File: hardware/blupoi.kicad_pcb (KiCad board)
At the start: 2 copper layers, 229.7 x 29.5 mm, 133 parts, among them P1 MICRO-B-USB, SW1 PM_BTN, U1 NRF52832, U2 TPS63031DSKR, U3 bno055, U4 ics43432, U5 BQ24075RGTT, U6 MAX16054AZT+T, U7 sip32408, X1 32MHz

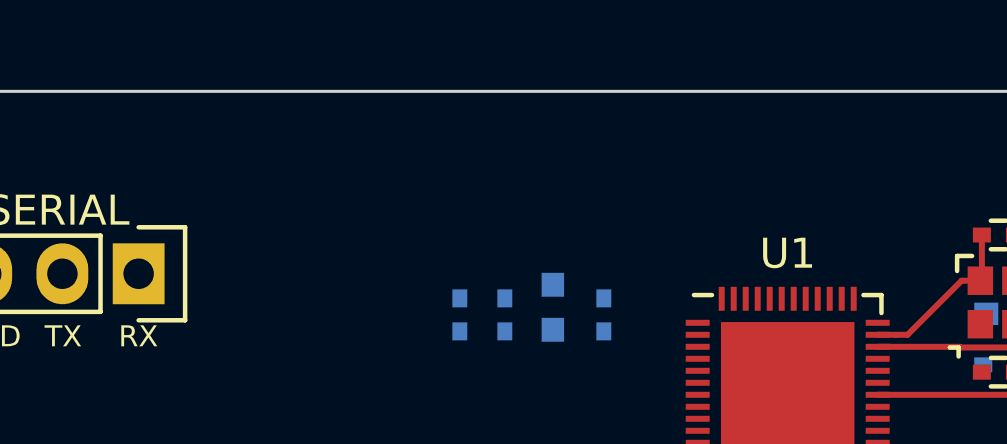
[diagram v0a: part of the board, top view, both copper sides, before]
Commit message: Added mode button
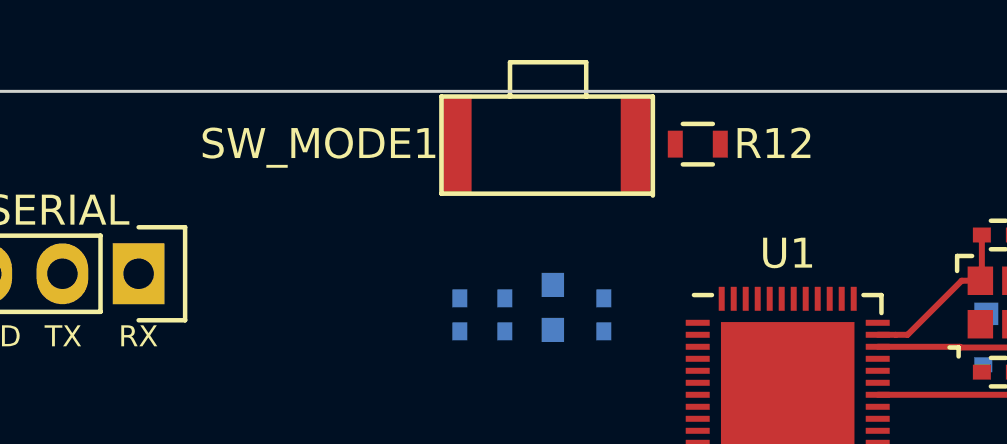
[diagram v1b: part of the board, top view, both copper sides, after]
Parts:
- added R12: 10k, Resistors_SMD:R_0603, F.Cu at (10.6, 94.9)
- added SW_MODE1: SW_SPST, kss241glfs:KSS241GLFS, F.Cu at (9.14, 96.5)
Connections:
- U6 pad 3: Net-(U6-Pad3) -> PM_SWITCH
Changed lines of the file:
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@@
-(kicad_pcb (version 20170123) (host pcbnew no-vcs-found-7652~57~ubuntu16.10.1)
+(kicad_pcb (version 20170123) (host pcbnew no-vcs-found-7663~57~ubuntu16.10.1)
   (general
-    (links 508)
-    (no_connects 436)
+    (links 512)
+    (no_connects 439)
     (area -60.860001 93.069999 168.980001 122.650001)
     (thickness 1.6)
@@
     (tracks 133)
     (zones 0)
-    (modules 133)
-    (nets 236)
+    (modules 135)
+    (nets 235)
   )
   (page A4)
@@
   )
   (setup
-    (last_trace_width 0.85)
+    (last_trace_width 0.2)
     (user_trace_width 0.2)
     (user_trace_width 0.25)
@@
   (net 226 "Net-(U3-Pad3)")
   (net 227 "Net-(U5-Pad14)")
-  (net 228 "Net-(U6-Pad3)")
-  (net 229 "Net-(U6-Pad4)")
-  (net 230 "Net-(U6-Pad5)")
-  (net 231 "Net-(U1-Pad11)")
-  (net 232 "Net-(U1-Pad12)")
-  (net 233 "Net-(U2-Pad4)")
-  (net 234 "Net-(U2-Pad2)")
-  (net 235 "Net-(U7-Pad2)")
+  (net 228 "Net-(U6-Pad4)")
+  (net 229 "Net-(U6-Pad5)")
+  (net 230 "Net-(U1-Pad11)")
+  (net 231 "Net-(U2-Pad4)")
+  (net 232 "Net-(U2-Pad2)")
+  (net 233 "Net-(U7-Pad2)")
+  (net 234 "Net-(R12-Pad1)")
   (net_class Default "This is the default net class."
     (clearance 0.2)
@@
     (add_net "Net-(R1-Pad1)")
     (add_net "Net-(R10-Pad1)")
+    (add_net "Net-(R12-Pad1)")
     (add_net "Net-(R2-Pad1)")
     (add_net "Net-(R3-Pad1)")
@@
     (add_net "Net-(U1-Pad10)")
     (add_net "Net-(U1-Pad11)")
-    (add_net "Net-(U1-Pad12)")
     (add_net "Net-(U1-Pad20)")
     (add_net "Net-(U1-Pad22)")
@@
     (add_net "Net-(U3-Pad6)")
     (add_net "Net-(U5-Pad14)")
-    (add_net "Net-(U6-Pad3)")
     (add_net "Net-(U6-Pad4)")
     (add_net "Net-(U6-Pad5)")
@@
       (net 212 "Net-(U1-Pad10)"))
     (pad 11 smd rect (at -3 1.8) (size 0.8 0.2) (layers F.Cu F.Paste F.Mask)
-      (net 231 "Net-(U1-Pad11)"))
+      (net 230 "Net-(U1-Pad11)"))
     (pad 12 smd rect (at -3 2.2) (size 0.8 0.2) (layers F.Cu F.Paste F.Mask)
-      (net 232 "Net-(U1-Pad12)") (clearance 0.001))
+      (net 234 "Net-(R12-Pad1)") (clearance 0.001))
     (pad 13 smd rect (at -2.2 3 90) (size 0.8 0.2) (layers F.Cu F.Paste F.Mask)
       (net 186 V3.3))
@@
       (net 184 VIN))
     (pad 4 smd oval (at 0.5 1.55 90) (size 0.28 1) (layers F.Cu F.Paste F.Mask)
-      (net 233 "Net-(U2-Pad4)"))
+      (net 231 "Net-(U2-Pad4)"))
     (pad 3 smd oval (at 0 1.55 90) (size 0.28 1) (layers F.Cu F.Paste F.Mask)
       (net 2 GND))
     (pad 2 smd oval (at -0.5 1.55 90) (size 0.28 1) (layers F.Cu F.Paste F.Mask)
-      (net 234 "Net-(U2-Pad2)"))
+      (net 232 "Net-(U2-Pad2)"))
     (pad 1 smd oval (at -1 1.55 90) (size 0.28 1) (layers F.Cu F.Paste F.Mask)
       (net 186 V3.3))
@@
       (net 2 GND) (clearance 0.14986))
     (pad 3 smd rect (at 0.94996 1.19888 180) (size 0.50038 0.8001) (layers F.Cu F.Paste F.Mask)
-      (net 228 "Net-(U6-Pad3)") (clearance 0.14986))
+      (net 192 PM_SWITCH) (clearance 0.14986))
     (pad 6 smd rect (at -0.94996 -1.19888 180) (size 0.50038 0.8001) (layers F.Cu F.Paste F.Mask)
       (net 185 VBAT) (clearance 0.14986))
     (pad 4 smd rect (at 0.94996 -1.19888 180) (size 0.50038 0.8001) (layers F.Cu F.Paste F.Mask)
-      (net 229 "Net-(U6-Pad4)") (clearance 0.14986))
+      (net 228 "Net-(U6-Pad4)") (clearance 0.14986))
     (pad 5 smd rect (at 0 -1.19888 180) (size 0.50038 0.8001) (layers F.Cu F.Paste F.Mask)
-      (net 230 "Net-(U6-Pad5)") (clearance 0.14986))
+      (net 229 "Net-(U6-Pad5)") (clearance 0.14986))
     (model ${KISYS3DMOD}/TO_SOT_Packages_SMD.3dshapes/SOT-23-6.wrl
       (at (xyz 0 0 0))
@@
     )
     (pad 2 smd rect (at -0.895 1.65 270) (size 0.3 0.7) (layers F.Cu F.Paste F.Mask)
-      (net 235 "Net-(U7-Pad2)"))
+      (net 233 "Net-(U7-Pad2)"))
     (pad 1 smd rect (at -0.395 1.65 270) (size 0.3 0.7) (layers F.Cu F.Paste F.Mask)
       (net 202 VCHG))
@@
       (net 184 VIN))
     (pad 3 smd rect (at -0.895 0 270) (size 0.3 0.7) (layers F.Cu F.Paste F.Mask)
-      (net 230 "Net-(U6-Pad5)"))
+      (net 229 "Net-(U6-Pad5)"))
     (pad 1 smd rect (at -0.645 0.825 270) (size 0.86 0.5) (layers F.Cu F.Paste F.Mask)
       (net 202 VCHG))
@@
     )
   )
+  (module Resistors_SMD:R_0603 (layer F.Cu)
+    (at 10.64 94.88)
+    (descr "Resistor SMD 0603, reflow soldering, Vishay (see dcrcw.pdf)")
+    (tags "resistor 0603")
+    (attr smd)
+    (fp_text reference R12 (at 2.54 0) (layer F.SilkS)
+      (effects (font (size 1 1) (thickness 0.15)))
+    )
+    (fp_text value 10k (at 0 1.9) (layer F.Fab)
+      (effects (font (size 1 1) (thickness 0.15)))
+    )
+    (fp_line (start -0.5 -0.675) (end 0.5 -0.675) (layer F.SilkS) (width 0.15))
+    (fp_line (start 0.5 0.675) (end -0.5 0.675) (layer F.SilkS) (width 0.15))
+    (fp_line (start 1.3 -0.8) (end 1.3 0.8) (layer F.CrtYd) (width 0.05))
+    (fp_line (start -1.3 -0.8) (end -1.3 0.8) (layer F.CrtYd) (width 0.05))
+    (fp_line (start -1.3 0.8) (end 1.3 0.8) (layer F.CrtYd) (width 0.05))
+    (fp_line (start -1.3 -0.8) (end 1.3 -0.8) (layer F.CrtYd) (width 0.05))
+    (fp_line (start -0.8 -0.4) (end 0.8 -0.4) (layer F.Fab) (width 0.1))
+    (fp_line (start 0.8 -0.4) (end 0.8 0.4) (layer F.Fab) (width 0.1))
+    (fp_line (start 0.8 0.4) (end -0.8 0.4) (layer F.Fab) (width 0.1))
+    (fp_line (start -0.8 0.4) (end -0.8 -0.4) (layer F.Fab) (width 0.1))
+    (pad 2 smd rect (at 0.75 0) (size 0.5 0.9) (layers F.Cu F.Paste F.Mask)
+      (net 2 GND))
+    (pad 1 smd rect (at -0.75 0) (size 0.5 0.9) (layers F.Cu F.Paste F.Mask)
+      (net 234 "Net-(R12-Pad1)"))
+    (model Resistors_SMD.3dshapes/R_0603.wrl
+      (at (xyz 0 0 0))
+      (scale (xyz 1 1 1))
+      (rotate (xyz 0 0 0))
+    )
+  )
+  (module kss241glfs:KSS241GLFS (layer F.Cu)
+    (at 9.1415 96.531 180)
+    (fp_text reference SW_MODE1 (at 11.1125 1.651 180) (layer F.SilkS)
+      (effects (font (size 1 1) (thickness 0.15)))
+    )
+    (fp_text value SW_SPST (at 0 -0.635 180) (layer F.Fab)
+      (effects (font (size 1 1) (thickness 0.15)))
+    )
+    (fp_line (start 4.7625 4.3815) (end 2.2225 4.3815) (layer F.SilkS) (width 0.15))
+    (fp_line (start 2.2225 4.3815) (end 2.2225 3.2385) (layer F.SilkS) (width 0.15))
+    (fp_line (start 4.7625 3.2385) (end 4.7625 4.3815) (layer F.SilkS) (width 0.15))
+    (fp_line (start 7.0485 0) (end 0 0) (layer F.SilkS) (width 0.15))
+    (fp_line (start 7.0485 3.2385) (end 7.0485 0) (layer F.SilkS) (width 0.15))
+    (fp_line (start 0 3.2385) (end 7.0485 3.2385) (layer F.SilkS) (width 0.15))
+    (fp_line (start 0 -0.0635) (end 0 3.2385) (layer F.SilkS) (width 0.15))
+    (pad 1 smd rect (at 0.5715 1.651 180) (size 1 3.3) (layers F.Cu F.Paste F.Mask)
+      (net 234 "Net-(R12-Pad1)"))
+    (pad 2 smd rect (at 6.5405 1.651 180) (size 1 3.3) (layers F.Cu F.Paste F.Mask)
+      (net 186 V3.3))
+  )
   (gr_line (start -46.07 122.6) (end 168.93 122.6) (layer Edge.Cuts) (width 0.1))

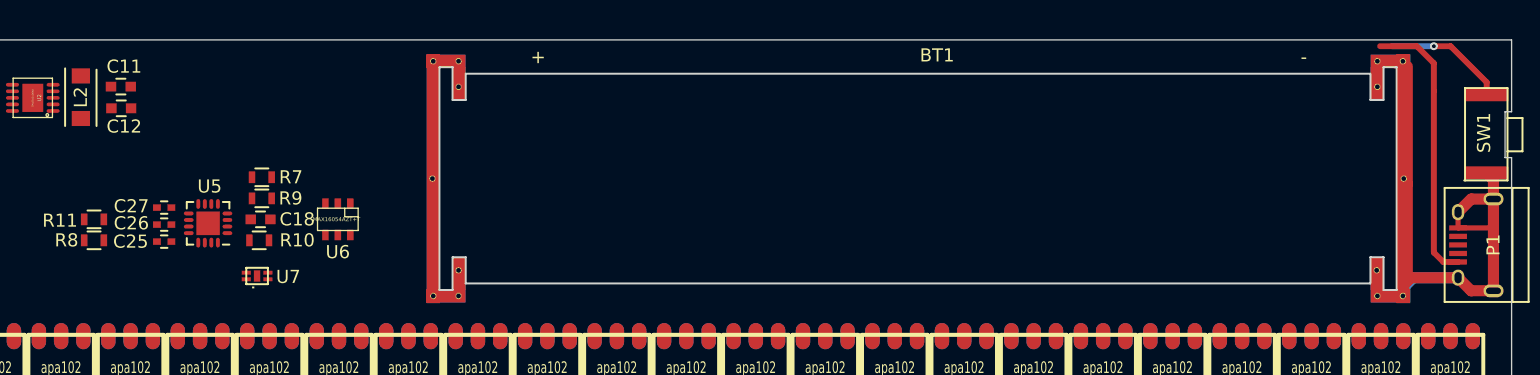
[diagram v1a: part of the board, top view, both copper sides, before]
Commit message: Fixed broken inductor schematic
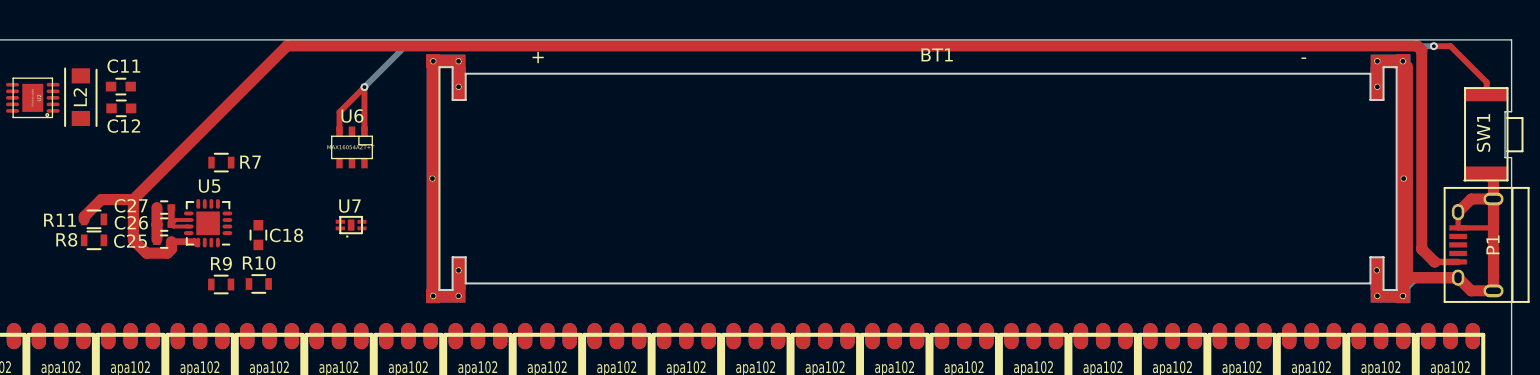
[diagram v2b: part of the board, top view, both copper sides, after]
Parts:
- moved U7 8.16 mm to (81.2, 107.9)
- moved R9 7.26 mm to (70.5, 111.8), turned to 180 degrees
- moved U6 5.59 mm to (80.5, 101.3)
- moved R10 3.33 mm to (73.3, 111.7)
- moved R7 3.29 mm to (70.5, 102.5)
- moved C18 1.21 mm to (73.3, 108.0), turned to 270 degrees
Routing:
- net VUSB: track 21.8 -> 136.0 mm
- net PM_SWITCH: track 9.32 -> 96.6 mm, vias 1 -> 2
- net VCHG: track 0.00 -> 4.16 mm
- net GND: track 76.4 -> 78.9 mm
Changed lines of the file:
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@@
     (thickness 1.6)
     (drawings 15)
-    (tracks 133)
+    (tracks 158)
     (zones 0)
     (modules 135)
@@
   )
   (setup
-    (last_trace_width 0.2)
+    (last_trace_width 0.45)
     (user_trace_width 0.2)
     (user_trace_width 0.25)
@@
   )
   (module Capacitors_SMD:C_0603 (layer F.Cu)
-    (at 73.48 106.81)
+    (at 73.32 108.01 270)
     (descr "Capacitor SMD 0603, reflow soldering, AVX (see smccp.pdf)")
     (tags "capacitor 0603")
     (attr smd)
-    (fp_text reference C18 (at 2.8 0 -180) (layer F.SilkS)
+    (fp_text reference C18 (at 0.06 -2.15 180) (layer F.SilkS)
       (effects (font (size 1 1) (thickness 0.15)))
     )
-    (fp_text value 47uF (at 0 1.9) (layer F.Fab)
+    (fp_text value 47uF (at 0 1.9 270) (layer F.Fab)
       (effects (font (size 1 1) (thickness 0.15)))
     )
@@
     (fp_line (start -0.35 -0.6) (end 0.35 -0.6) (layer F.SilkS) (width 0.15))
     (fp_line (start 0.35 0.6) (end -0.35 0.6) (layer F.SilkS) (width 0.15))
-    (pad 1 smd rect (at -0.75 0) (size 0.8 0.75) (layers F.Cu F.Paste F.Mask)
+    (pad 1 smd rect (at -0.75 0 270) (size 0.8 0.75) (layers F.Cu F.Paste F.Mask)
       (net 185 VBAT))
-    (pad 2 smd rect (at 0.75 0) (size 0.8 0.75) (layers F.Cu F.Paste F.Mask)
+    (pad 2 smd rect (at 0.75 0 270) (size 0.8 0.75) (layers F.Cu F.Paste F.Mask)
       (net 2 GND))
     (model Capacitors_SMD.3dshapes/C_0603.wrl
@@
   )
   (module Resistors_SMD:R_0603 (layer F.Cu)
-    (at 73.58 105.21)
+    (at 70.48 111.78 180)
     (descr "Resistor SMD 0603, reflow soldering, Vishay (see dcrcw.pdf)")
     (tags "resistor 0603")
     (attr smd)
-    (fp_text reference R9 (at 2.2 0) (layer F.SilkS)
+    (fp_text reference R9 (at 0 1.55 180) (layer F.SilkS)
       (effects (font (size 1 1) (thickness 0.15)))
     )
-    (fp_text value 590 (at 0 1.9) (layer F.Fab)
+    (fp_text value 590 (at 0 1.9 180) (layer F.Fab)
       (effects (font (size 1 1) (thickness 0.15)))
     )
@@
     (fp_line (start 0.5 0.675) (end -0.5 0.675) (layer F.SilkS) (width 0.15))
     (fp_line (start -0.5 -0.675) (end 0.5 -0.675) (layer F.SilkS) (width 0.15))
-    (pad 1 smd rect (at -0.75 0) (size 0.5 0.9) (layers F.Cu F.Paste F.Mask)
+    (pad 1 smd rect (at -0.75 0 180) (size 0.5 0.9) (layers F.Cu F.Paste F.Mask)
       (net 189 PM_ISET))
-    (pad 2 smd rect (at 0.75 0) (size 0.5 0.9) (layers F.Cu F.Paste F.Mask)
+    (pad 2 smd rect (at 0.75 0 180) (size 0.5 0.9) (layers F.Cu F.Paste F.Mask)
       (net 2 GND))
     (model Resistors_SMD.3dshapes/R_0603.wrl
@@
   )
   (module Resistors_SMD:R_0603 (layer F.Cu)
-    (at 73.38 108.41)
+    (at 73.35 111.74)
     (descr "Resistor SMD 0603, reflow soldering, Vishay (see dcrcw.pdf)")
     (tags "resistor 0603")
     (attr smd)
-    (fp_text reference R10 (at 2.9 0) (layer F.SilkS)
+    (fp_text reference R10 (at 0 -1.56) (layer F.SilkS)
       (effects (font (size 1 1) (thickness 0.15)))
     )
@@
   )
   (module tinkerforge-libraries:SOT23-6 (layer F.Cu)
-    (at 79.38 106.81 180)
-    (fp_text reference U6 (at 0 -2.5 180) (layer F.SilkS)
+    (at 80.46004 101.32112 180)
+    (fp_text reference U6 (at -0.02 2.36 180) (layer F.SilkS)
       (effects (font (size 1 1) (thickness 0.15)))
     )
@@
   )
   (module Resistors_SMD:R_0603 (layer F.Cu)
-    (at 73.58 103.6)
+    (at 70.49 102.48)
     (descr "Resistor SMD 0603, reflow soldering, Vishay (see dcrcw.pdf)")
     (tags "resistor 0603")
@@
   )
   (module sip32408:sip32408 (layer F.Cu)
-    (at 74.045 111.775 270)
-    (fp_text reference U7 (at -0.575 -1.555) (layer F.SilkS)
+    (at 81.22 107.89 270)
+    (fp_text reference U7 (at -2.065 0.915) (layer F.SilkS)
       (effects (font (size 1 1) (thickness 0.15)))
     )
@@
   (segment (start 29.056 101.479414) (end 29.056 103.286) (width 0.2) (layer F.Cu) (net 1))
   (segment (start 29.056 103.286) (end 29.07 103.3) (width 0.2) (layer F.Cu) (net 1))
+  (segment (start 65.58 107.21) (end 65.58 108.334991) (width 0.85) (layer F.Cu) (net 2))
+  (segment (start 65.58 105.91) (end 65.58 107.21) (width 0.85) (layer F.Cu) (net 2))
   (segment (start 160.6365 112.6535) (end 160.6365 111.836) (width 0.85) (layer F.Cu) (net 2))
   (segment (start 160.6365 111.836) (end 161.2116 111.2609) (width 0.85) (layer F.Cu) (net 2))
@@
   (segment (start -0.858 109.614) (end -1.958 109.614) (width 0.2) (layer F.Cu) (net 186))
   (segment (start -1.958 109.614) (end -2.008 109.664) (width 0.2) (layer F.Cu) (net 186))
-  (segment (start 161.7 93.6) (end 158.9 93.6) (width 0.45) (layer F.Cu) (net 187))
-  (segment (start 163 94.9) (end 161.7 93.6) (width 0.45) (layer F.Cu) (net 187))
-  (segment (start 163 97) (end 163 94.9) (width 0.45) (layer F.Cu) (net 187))
-  (segment (start 164.84746 110.0609) (end 163.72246 110.0609) (width 0.45) (layer F.Cu) (net 187))
+  (segment (start 66.68 108.51) (end 68.45498 108.51) (width 0.5) (layer F.Cu) (net 187))
+  (segment (start 68.45498 108.51) (end 68.62999 108.68501) (width 0.5) (layer F.Cu) (net 187))
+  (segment (start 63.78 105.3) (end 63.78 108.385002) (width 0.85) (layer F.Cu) (net 187))
+  (segment (start 63.78 108.385002) (end 64.779999 109.385001) (width 0.85) (layer F.Cu) (net 187))
+  (segment (start 64.779999 109.385001) (end 66.380001 109.385001) (width 0.85) (layer F.Cu) (net 187))
+  (segment (start 66.380001 109.385001) (end 66.68 109.085002) (width 0.85) (layer F.Cu) (net 187))
+  (segment (start 66.68 109.085002) (end 66.68 108.51) (width 0.85) (layer F.Cu) (net 187))
+  (segment (start 163.0991 110.0609) (end 163.0509 110.0609) (width 0.85) (layer F.Cu) (net 187))
+  (segment (start 163.0509 110.0609) (end 162.074999 109.084999) (width 0.85) (layer F.Cu) (net 187))
+  (segment (start 162.074999 93.924999) (end 161.724999 93.574999) (width 0.85) (layer F.Cu) (net 187))
+  (segment (start 162.074999 109.084999) (end 162.074999 93.924999) (width 0.85) (layer F.Cu) (net 187))
+  (segment (start 161.724999 93.574999) (end 75.505001 93.574999) (width 0.85) (layer F.Cu) (net 187))
+  (segment (start 75.505001 93.574999) (end 63.78 105.3) (width 0.85) (layer F.Cu) (net 187))
+  (segment (start 61.34 105.3) (end 60.03 106.61) (width 0.85) (layer F.Cu) (net 187))
+  (segment (start 60.03 106.61) (end 60.03 106.81) (width 0.85) (layer F.Cu) (net 187))
+  (segment (start 63.78 105.3) (end 61.34 105.3) (width 0.85) (layer F.Cu) (net 187))
+  (segment (start 164.84746 110.0609) (end 163.0991 110.0609) (width 0.5) (layer F.Cu) (net 187))
+  (segment (start 68.62999 108.68501) (end 68.62999 108.585) (width 0.5) (layer F.Cu) (net 187))
   (segment (start 164.84746 110.0609) (end 164.2391 110.0609) (width 0.45) (layer F.Cu) (net 187))
-  (segment (start 163 109.33844) (end 163 97) (width 0.45) (layer F.Cu) (net 187))
-  (segment (start 163.72246 110.0609) (end 163 109.33844) (width 0.45) (layer F.Cu) (net 187))
+  (segment (start 81.41 96.72) (end 79.51008 98.61992) (width 0.45) (layer F.Cu) (net 192))
+  (segment (start 79.51008 98.61992) (end 79.51008 100.12224) (width 0.45) (layer F.Cu) (net 192))
+  (segment (start 81.41 100.12224) (end 81.41 96.72) (width 0.45) (layer F.Cu) (net 192))
+  (via (at 81.41 96.72) (size 0.6) (drill 0.3) (layers F.Cu B.Cu) (net 192))
+  (segment (start 84.53 93.6) (end 81.41 96.72) (width 0.45) (layer B.Cu) (net 192))
+  (segment (start 159.8 93.6) (end 84.53 93.6) (width 0.45) (layer B.Cu) (net 192))
   (segment (start 163 93.6) (end 159.8 93.6) (width 0.45) (layer B.Cu) (net 192))
   (segment (start 167.03 97.301) (end 167.03 96.351) (width 0.45) (layer F.Cu) (net 192))
@@
   (segment (start 164.279 93.6) (end 163 93.6) (width 0.45) (layer F.Cu) (net 192))
   (via (at 163 93.6) (size 0.6) (drill 0.3) (layers F.Cu B.Cu) (net 192))
+  (segment (start 66.68 105.91) (end 66.68 107.21) (width 0.5) (layer F.Cu) (net 202))
+  (segment (start 68.005 106.86) (end 67.03 106.86) (width 0.3) (layer F.Cu) (net 202))
+  (segment (start 67.03 106.86) (end 66.68 107.21) (width 0.3) (layer F.Cu) (net 202))
+  (segment (start 68.005 107.36) (end 66.83 107.36) (width 0.3) (layer F.Cu) (net 202))
+  (segment (start 66.83 107.36) (end 66.68 107.21) (width 0.3) (layer F.Cu) (net 202))
   (segment (start -42.43 120.52) (end -42.43 120.07) (width 0.2) (layer B.Cu) (net 204))
   (zone (net 0) (net_name "") (layer F.Cu) (hatch edge 0.508)
